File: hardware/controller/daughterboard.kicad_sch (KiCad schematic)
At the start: 5 parts, among them J1 TYPE-C-31-D-06, J8 J_DB 1x10 P1.00mm, U3 TPD4E05U06DQAR

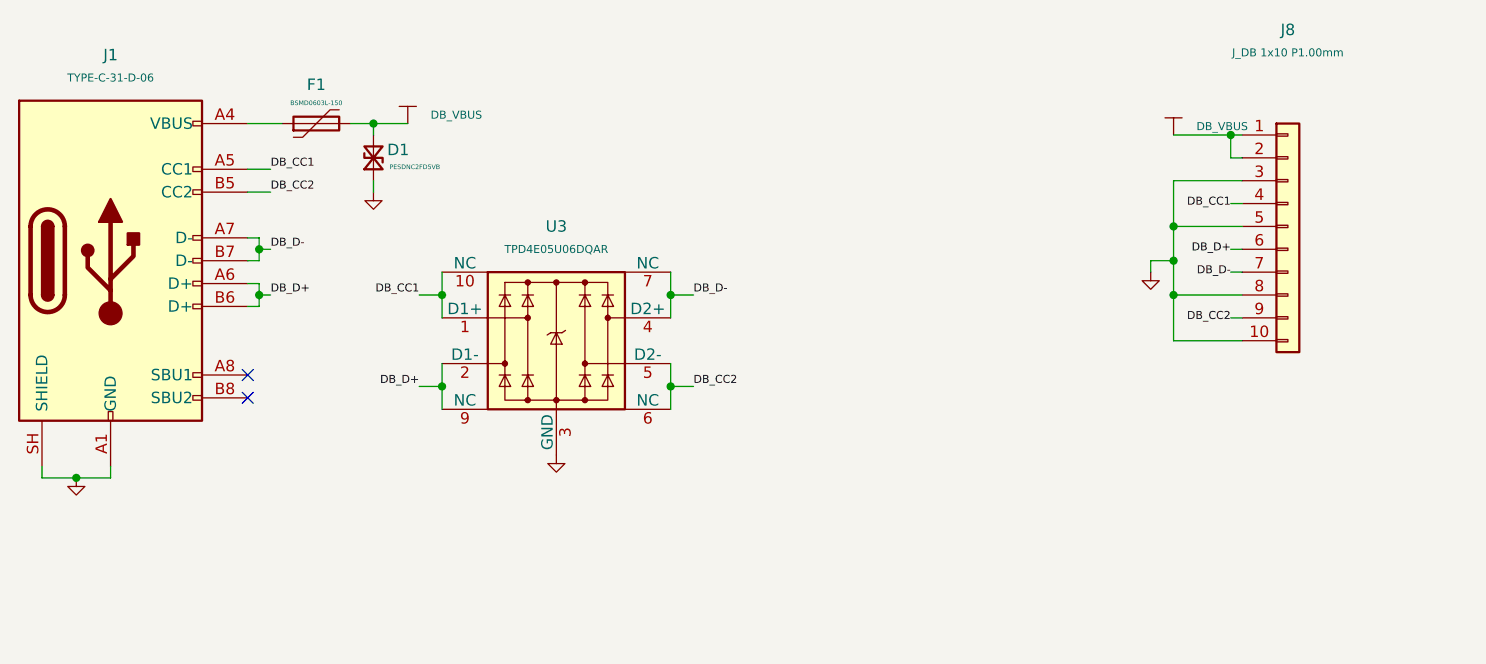
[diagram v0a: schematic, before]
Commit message: feat(controller): MB cleanup before ERC, Q1 PMPB15XP, Y1 NX2016SA, MB-DB pinout (A12, P9, M1, I6)
- no-connects on unused nRF52840 and nPM1300 pins; C10, C13, BT1 removed;
  C22 DNP; PVSS2 drawn with new easyeda2kicad:pgnd; J5 as Conn_01x01;
  J2 as Conn_01x02_MountingPin
- Q1: Nexperia PMPB15XP,115 (C513107), new ibm_m:PMPB15XP symbol,
  DFN2020MD-6 footprint and 3D model imported via easyeda2kicad
- Y1: NDK NX2016SA-32MHZ-EXS00A-CS06654 (C5441424), CL 8 pF
- J8/J9 pinout: VBUS, VBUS, CC1, GND, D+, D-, GND, CC2, GND, GND
- easyeda2kicad.kicad_sym: remove premature closing paren that hid 10 symbols
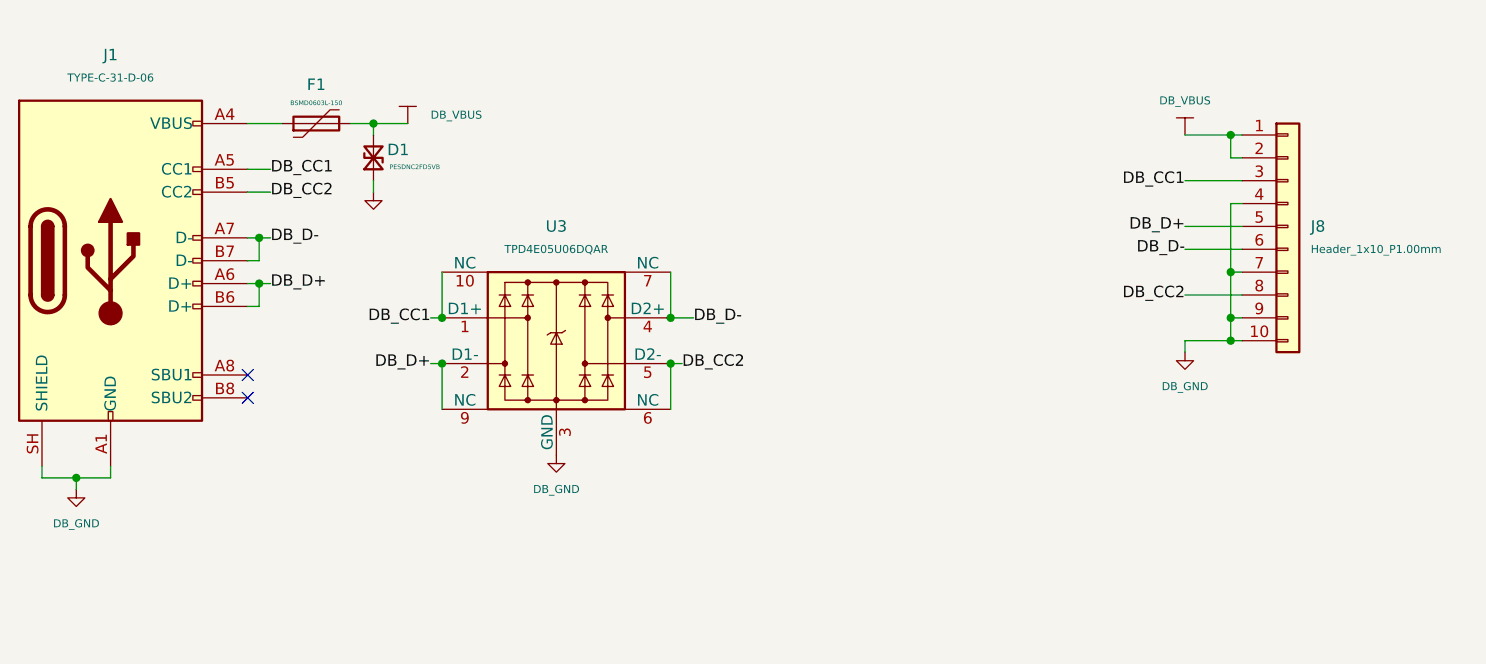
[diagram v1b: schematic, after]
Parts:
- J8: value J_DB 1x10 P1.00mm -> Header_1x10_P1.00mm; footprint Connector_PinHeader_1.00mm:PinHeader_1x10_P1.00mm_Vertical_SMD_Pin1Left -> Connector_PinHeader_1.00mm:PinHeader_1x10_P1.00mm_Vertical
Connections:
- net DB_CC1: now also J8.3 (Pin_3); no longer J8.4 (Pin_4)
- net DB_CC2: now also J8.8 (Pin_8); no longer J8.9 (Pin_9)
- net DB_D+: now also J8.5 (Pin_5); no longer J8.6 (Pin_6)
- net DB_D-: now also J8.6 (Pin_6); no longer J8.7 (Pin_7)
- net DB_GND: now also J8.4 (Pin_4), J8.7 (Pin_7), J8.9 (Pin_9); no longer J8.3 (Pin_3), J8.5 (Pin_5), J8.8 (Pin_8)

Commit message: feat(controller): VBUS protection F1/D1, TPD4E05U06 symbol, ERC power flags (I3)
- F1 SMD1210-110-24V (C22436715), D1 SMF20A (C123788) as D_Zener_Small, cathode on DB_VBUS
- U3 on new ibm_m:TPD4E05U06DQA symbol, connections unchanged
- ERC sheet with PWR_FLAG for VBUS, VBAT, PVSS2, DB_VBUS, DB_GND
- C19 footprint 0402
- docs: I3 applied, J2 = JST PH, WS2812C VIH resolved
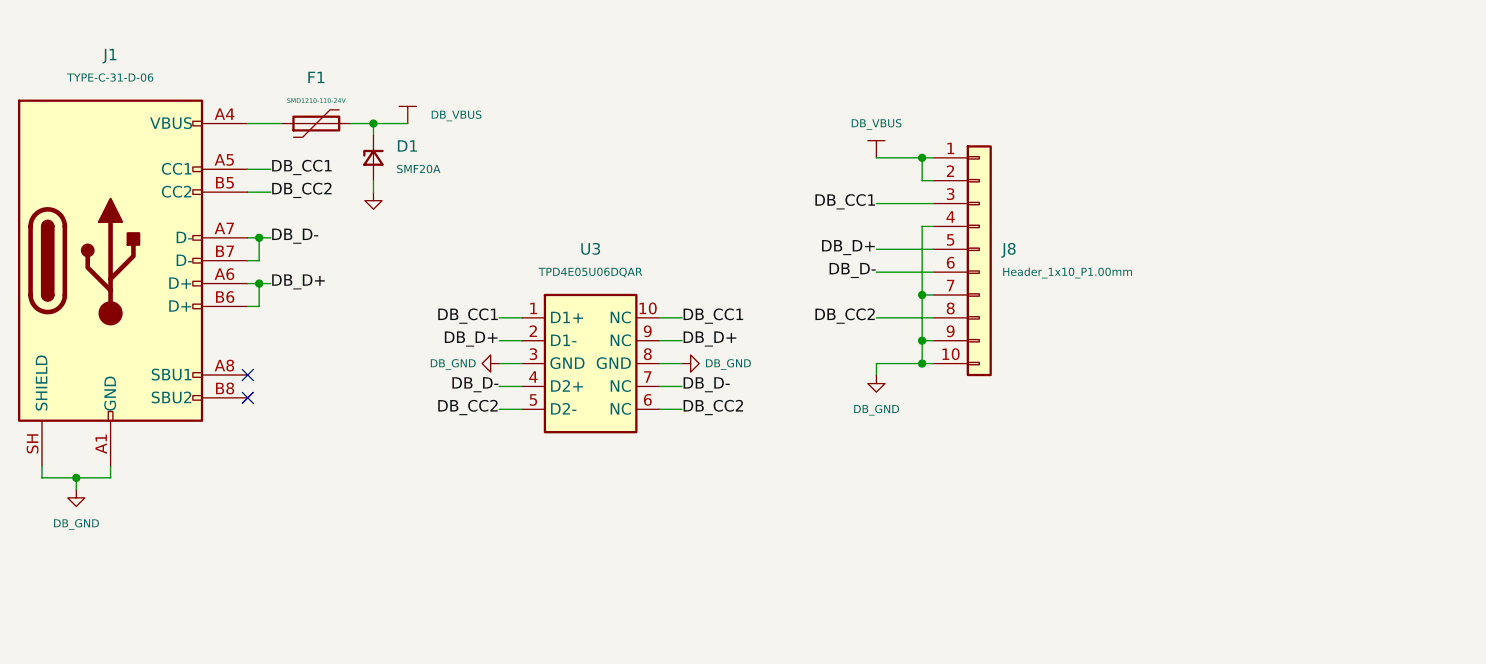
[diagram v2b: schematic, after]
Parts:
- D1: value PESDNC2FD5VB -> SMF20A; footprint easyeda2kicad:Diodes_DFN1006-2 -> Diode_SMD:D_SOD-123F; symbol Device:D_TVS_Small -> Device:D_Zener_Small; LCSC Part C110694 -> C123788
- F1: value BSMD0603L-150 -> SMD1210-110-24V; footprint Fuse:Fuse_0603_1608Metric -> Fuse:Fuse_1210_3225Metric; LCSC Part C914094 -> C22436715
- U3: symbol Power_Protection:TPD4E05U06DQA -> ibm_m:TPD4E05U06DQA
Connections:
- net DB_GND: now also D1.2 (A); no longer D1.1 (A1)
- net DB_VBUS: now also D1.1 (K); no longer D1.2 (A2)
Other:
- moved on the sheet: J8

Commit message: feat(controller): split schematic into pages, JLC BOM, RF config 7 (A13, A14, M5, P9)
- Schematic split into Power, MCU Core, MCU IO and Daughterboard pages;
  motherboard.kicad_sch and ERC.kicad_sch removed, cross-page signals as
  global labels. J3 pins 1-3 fixed (local labels did not join power nets).
- R1/R2 0R in series with SCL/SDA to J3.
- RF matching per nRF52840 reference config 7 (C3 1.0p, L1 4.7n, C4 1.2p,
  L5 2.2n), C22 removed.
- BOM for JLC assembly: passives moved to basic parts, R10 LCSC fixed
  (470k 0603), C16 0603, C9 DNP; Q2 AO3401A (new ibm_m symbol);
  SW1 TS-1187A-B-A-B; D2 WS2812B-2020-V6; J6 U.FL-IPEX-1 (pads renumbered).
- ERC 0 errors / 0 warnings; tools/kicad-check.sh runs ERC, netlist, PDF.
- Docs: CHANGELOG A13/A14, M5, P9; HARDWARE_DECISIONS BOM table; CLAUDE.md.
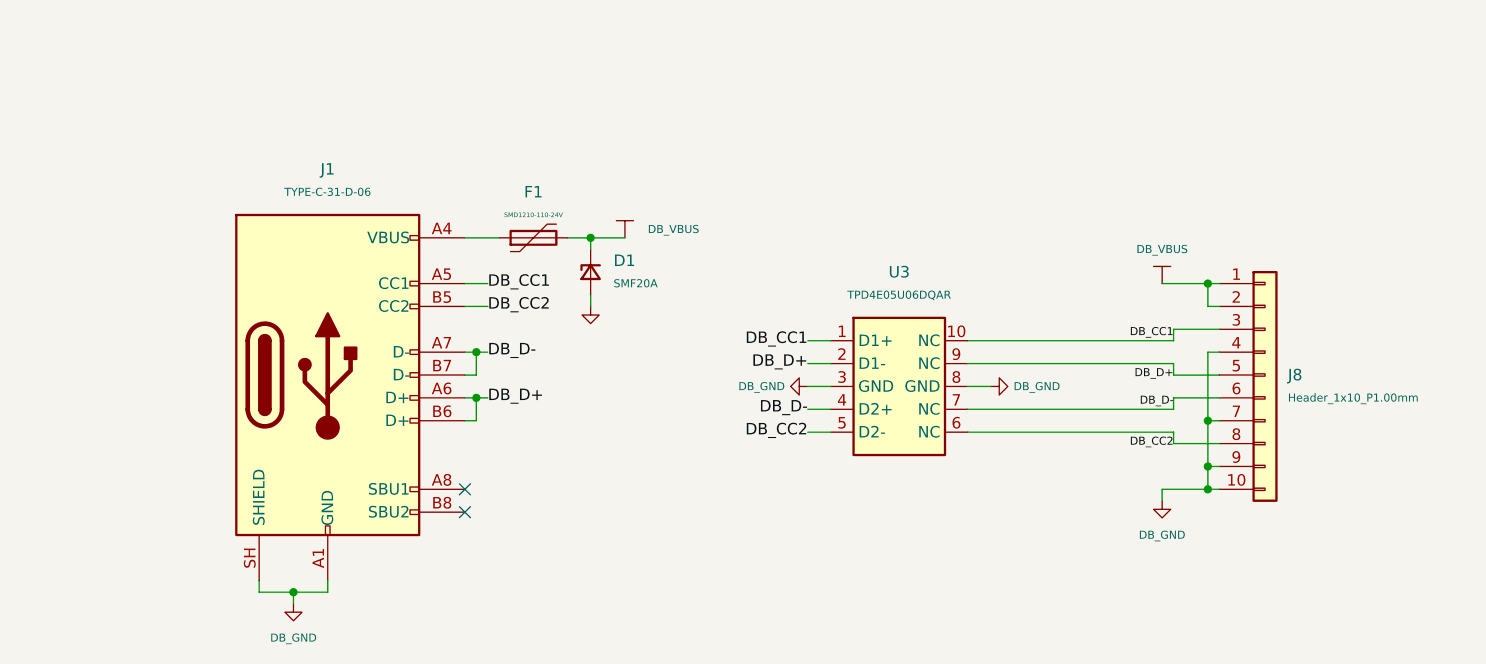
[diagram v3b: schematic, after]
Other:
- title: (none) -> IBM Model M Controller
- moved on the sheet: D1, F1, J1, J8, U3

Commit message: feat(controller): update PCB from schematic, footprint cleanup, DRC in check script
- PCB updated from the split schematic: new parts placed (C19, C35, D2, J3,
  L5, NT1, Q2, R1/R2, R11/R12, SW1, TP1), old ones removed (D4, D92,
  SW89-91, old Q1, C10), footprints replaced (J2 JST PH, J8/J9 1x10 1.0 mm,
  F1 1210, D1 SOD-123F).
- Footprint fixes: J1 shield pads, pad rounding, silkscreen; standard
  footprints with local changes copied to ibm_bs.pretty (JST PH, headers,
  SOT-23, test pad).
- tools/kicad-check.sh: PCB DRC with schematic parity.
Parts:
- J8: footprint Connector_PinHeader_1.00mm:PinHeader_1x10_P1.00mm_Vertical -> ibm_bs:PinHeader_1x10_P1.00mm_Vertical_SMD_Pin1Left
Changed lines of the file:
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@@
 			)
 		)
-		(property "Footprint" "Connector_PinHeader_1.00mm:PinHeader_1x10_P1.00mm_Vertical"
+		(property "Footprint" "ibm_bs:PinHeader_1x10_P1.00mm_Vertical_SMD_Pin1Left"
 			(at 203.2 101.6 0)
 			(hide yes)
